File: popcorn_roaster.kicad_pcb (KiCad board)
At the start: 2 copper layers, 105.8 x 77.9 mm, 38 parts, among them Q1 BC847B, U1 R-78K3.3-0.5, U2 IRM-45-24, U3 MOC3063S, U4 MAX31855

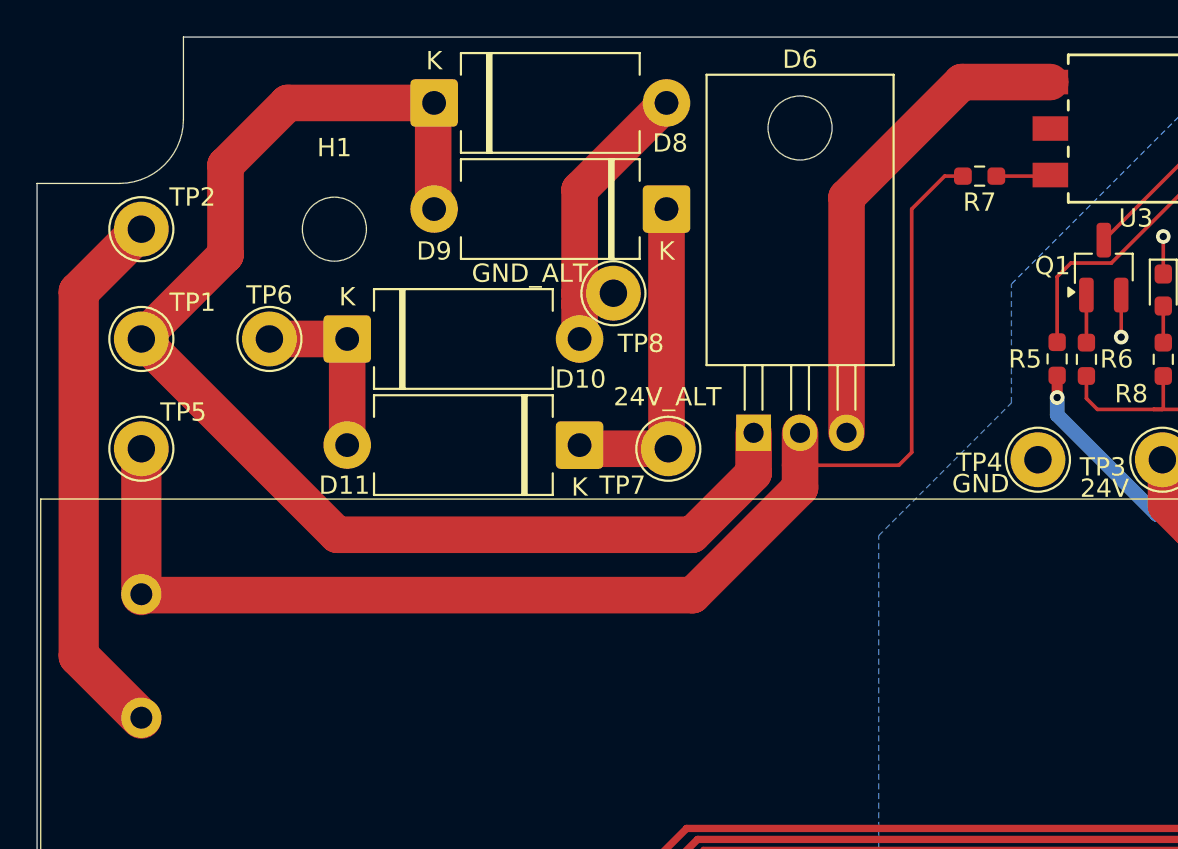
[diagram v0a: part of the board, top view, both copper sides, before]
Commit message: Add clearance rules for AC mains lines
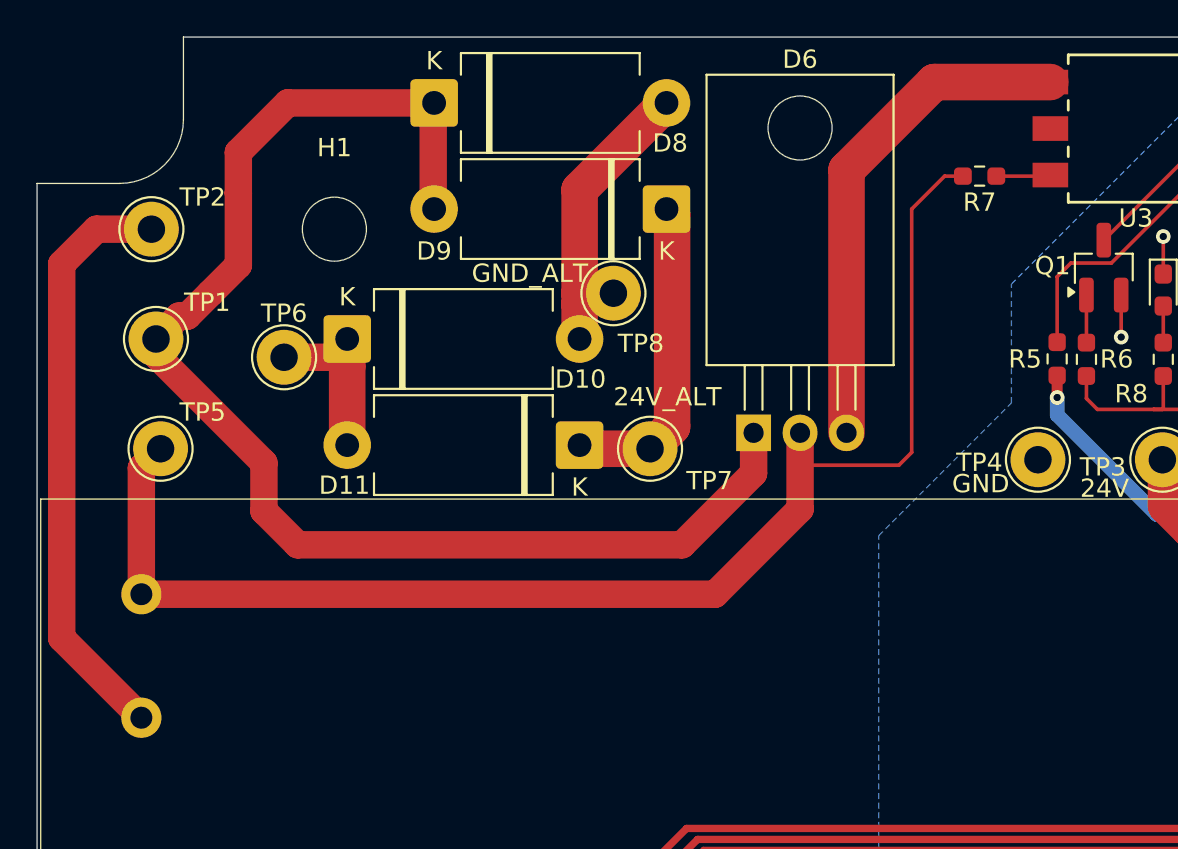
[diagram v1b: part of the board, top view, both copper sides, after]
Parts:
- moved TP6 1.28 mm to (13.5, 17.5)
- moved TP5 1.05 mm to (6.75, 22.5)
- moved TP7 1.00 mm to (33.5, 22.5)
- moved TP1 0.80 mm to (6.50, 16.5)
- moved TP2 0.55 mm to (6.25, 10.5)
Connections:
- net Net-(D6-G) renamed /Smart Roaster/triac_g
- net Net-(U3-A2) renamed /Smart Roaster/triac_a2
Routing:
- net /Smart Roaster/N (blue): track 29.6 -> 32.1 mm
- net /Smart Roaster/heat_blue: track 71.5 -> 73.1 mm
- net /Smart Roaster/heat_black: track 72.7 -> 73.8 mm
- net /Smart Roaster/triac_g: track 26.6 -> 27.5 mm
